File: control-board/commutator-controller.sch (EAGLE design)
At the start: 41 parts, among them U1 PTN04050C, U2 LTC4425EMSE#PBF, U3 IS31FL3193, U4 TMC2130, U5 TEENSY_LC

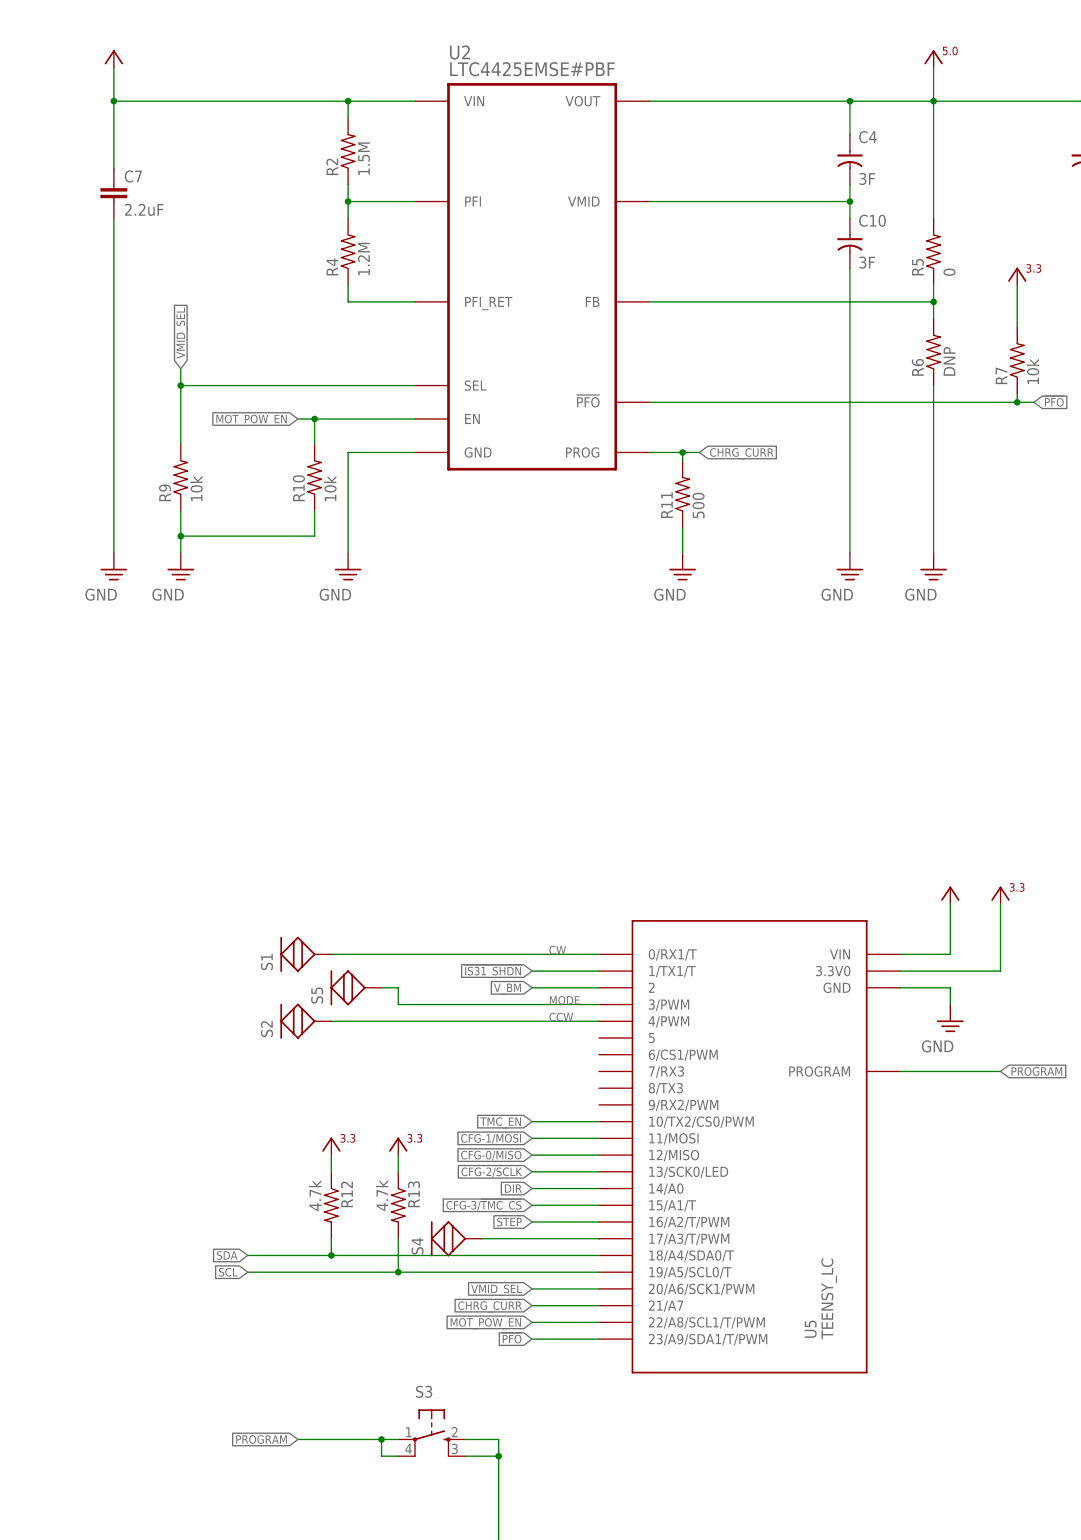
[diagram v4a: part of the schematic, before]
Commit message: Updates to README, firmware, and control-board
- Fixed mirrored pads for super capacitor charger
- Switched Teensy LC for Teensy 3.2
- Moved Teensy in 2mm so that housing does not need large cutout, but
small one for micro USB
- Fixed other small issues with the circuit
- Some small changed to firmware: speed now provided directly in RPM
instead of scale factor. Boundary checks on values. Some other things
too.
- Updated README
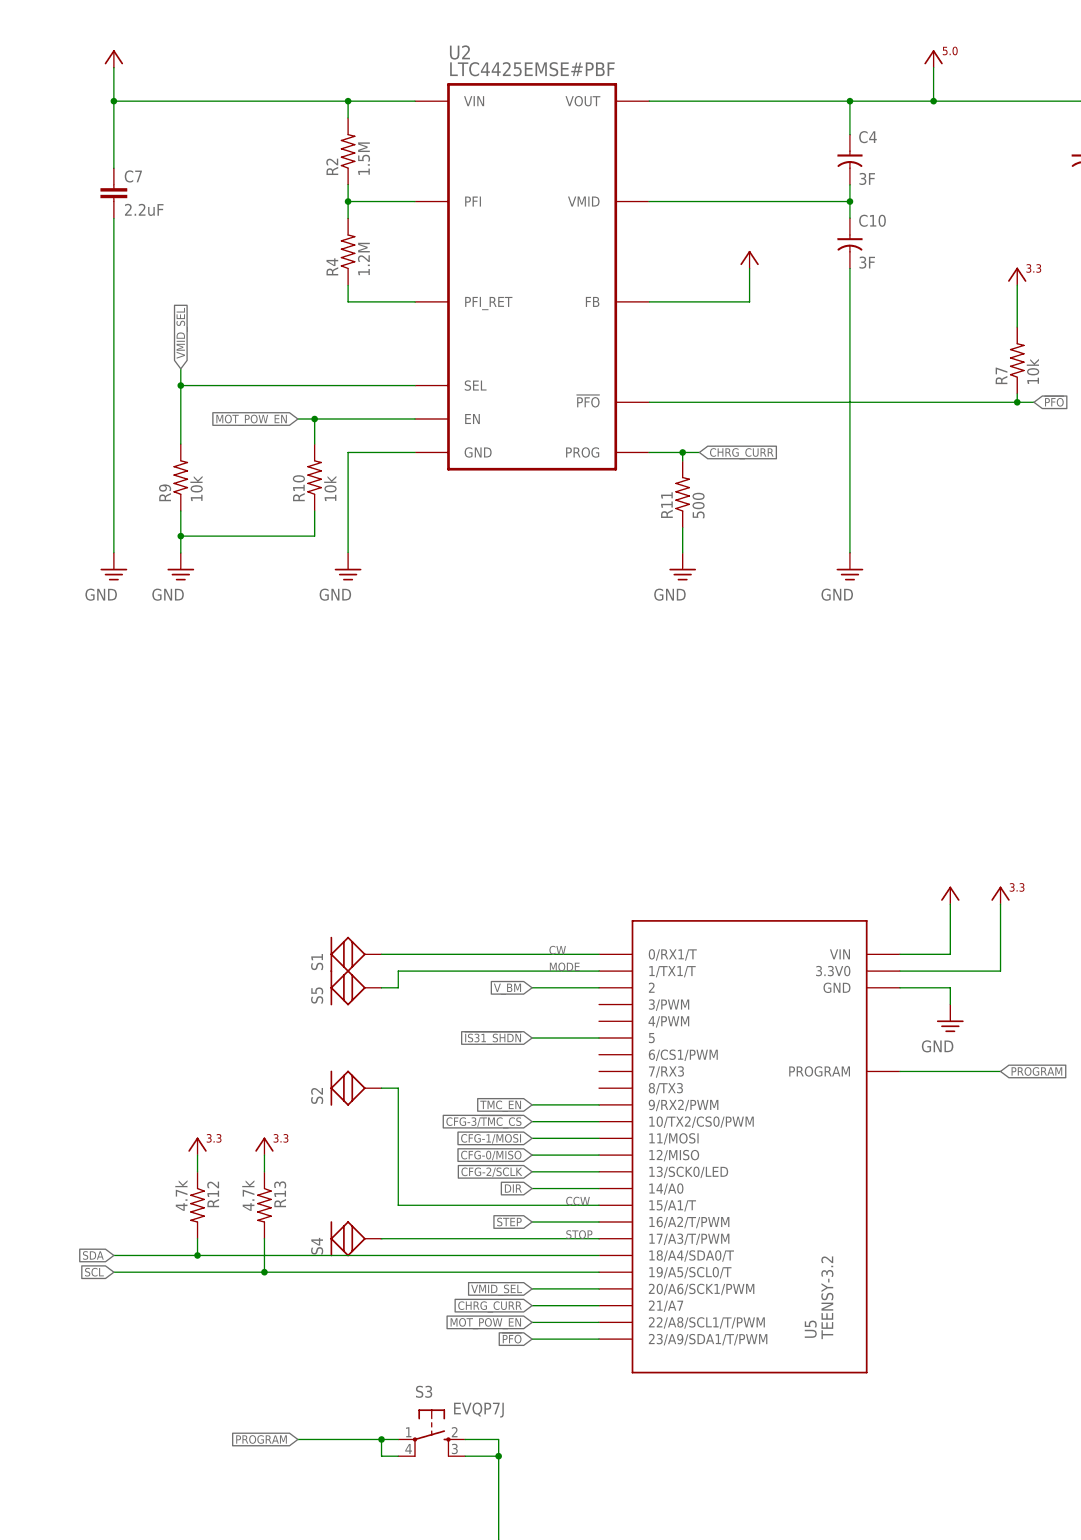
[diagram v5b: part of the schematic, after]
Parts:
- removed R5: 0, jonnew:R_0603
- removed R6: DNP, jonnew:R_0603
- C8: device jonnew:C_0402 -> jonnew:C_0603
- S3: value (none) -> EVQP7J
- U5: value TEENSY_LC -> TEENSY-3.2
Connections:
- removed net N$4: R5.1, R6.2, U2.FB
- net !IS31_SHDN: now also U5.5; no longer U5.1/TX1/T
- net +5V0: no longer R5.2
- net CCW: now also U5.15/A1/T; no longer U5.4/PWM
- net CFG-3/!TMC_CS: now also U5.10/TX2/CS0/PWM; no longer U5.15/A1/T
- net GND: no longer R6.1
- net MODE: now also U5.1/TX1/T; no longer U5.3/PWM
- net TMC_EN: now also U5.9/RX2/PWM; no longer U5.10/TX2/CS0/PWM
- net VCC: now also U2.FB
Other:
- moved on the sheet: R12, R13, S1, S2, S4
